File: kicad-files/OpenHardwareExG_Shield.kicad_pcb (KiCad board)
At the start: 4 copper layers, 125.1 x 59.7 mm, 196 parts, among them P1 CONN_1, P10 CONN_18, P11 CONN_1, P12 CONN_1, P13 CONN_1, P14 CONN_1, P15 CONN_1, P16 CONN_1, P17 CONN_1, P18 CONN_1, P19 ARDUINO_SHIELD, P2 CONN_1, P20 CONN_3X2, P21 CONN_3X2, P22 CONN_7, P23 CONN_1, P24 CONN_1, P25 CONN_1, P26 CONN_1, P27 CONN_1, P28 CONN_1, P29 CONN_1, P3 CONN_1, P30 CONN_1, P31 CONN_1, P32 CONN_1, P33 CONN_1, P34 CONN_1, P35 CONN_1, P36 CONN_1, P37 CONN_1, P38 CONN_1, P39 CONN_1, P4 CONN_1, P40 CONN_1, P41 CONN_1, P42 CONN_1, P43 CONN_1, P44 CONN_1, P45 CONN_1, P46 CONN_1, P47 CONN_1, P48 CONN_1, P49 CONN_1, P5 CONN_1, P50 CONN_1, P51 CONN_1, P52 CONN_1, P53 CONN_1, P54 CONN_1, P55 CONN_1, P6 CONN_1, P7 CONN_1, P8 CONN_1, P9 CONN_1, U1 ADS1299, U2 Z0109MNT1G, U3 TL431BIDBZR, U4 873-AAT3220IGY-33T1, U5 ADUM6000, U6 SI8663, U7 74LS02, U8 74LS00, U9 74LS125

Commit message: connect DGND_ISO to DGND (DOH!); convert to KiCad 4
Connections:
- P19 pad 0: (no net) -> Net-(P19-Pad0)
- P19 pad 1: (no net) -> Net-(P19-Pad1)
- P19 pad 10: (no net) -> Net-(P19-Pad10)
- P19 pad 11: (no net) -> Net-(P19-Pad11)
- P19 pad 12: (no net) -> Net-(P19-Pad12)
- P19 pad 13: (no net) -> Net-(P19-Pad13)
- P19 pad 2: (no net) -> Net-(P19-Pad2)
- P19 pad 3: (no net) -> Net-(P19-Pad3)
- P19 pad 4: (no net) -> Net-(P19-Pad4)
- P19 pad 54: (no net) -> Net-(P19-Pad54)
- P19 pad 55: (no net) -> Net-(P19-Pad55)
- P19 pad 56: (no net) -> Net-(P19-Pad56)
- P19 pad 57: (no net) -> Net-(P19-Pad57)
- P19 pad 58: (no net) -> Net-(P19-Pad58)
- P19 pad 59: (no net) -> Net-(P19-Pad59)
- P19 pad 70: (no net) -> Net-(P19-Pad70)
- P19 pad 71: (no net) -> Net-(P19-Pad71)
- P19 pad 8: (no net) -> Net-(P19-Pad8)
- P19 pad 88: (no net) -> Net-(P19-Pad88)
- P19 pad 89: (no net) -> Net-(P19-Pad89)
- P19 pad 9: (no net) -> Net-(P19-Pad9)
- P19 pad 90: (no net) -> Net-(P19-Pad90)
- P19 pad 92: (no net) -> Net-(P19-Pad92)
- P19 pad 97: (no net) -> Net-(P19-Pad97)
- P19 pad 98: (no net) -> Net-(P19-Pad98)
- P22 pad 5: /DGND_ISO -> AGND
- P31 pad 1: /DGND_ISO -> AGND
- U1 pad 17: (no net) -> Net-(U1-Pad17)
- U1 pad 18: (no net) -> Net-(U1-Pad18)
- U1 pad 27: (no net) -> Net-(U1-Pad27)
- U1 pad 29: (no net) -> Net-(U1-Pad29)
- U1 pad 60: (no net) -> Net-(U1-Pad60)
- U1 pad 62: (no net) -> Net-(U1-Pad62)
- U1 pad 64: (no net) -> Net-(U1-Pad64)
- U5 pad 11: (no net) -> Net-(U5-Pad11)
- U5 pad 12: (no net) -> Net-(U5-Pad12)
- U5 pad 4: (no net) -> Net-(U5-Pad4)
- U5 pad 5: (no net) -> Net-(U5-Pad5)
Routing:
- net AGND: track 160.0 -> 162.5 mm
- net /DGND_ISO: track 2.54 -> 0.00 mm

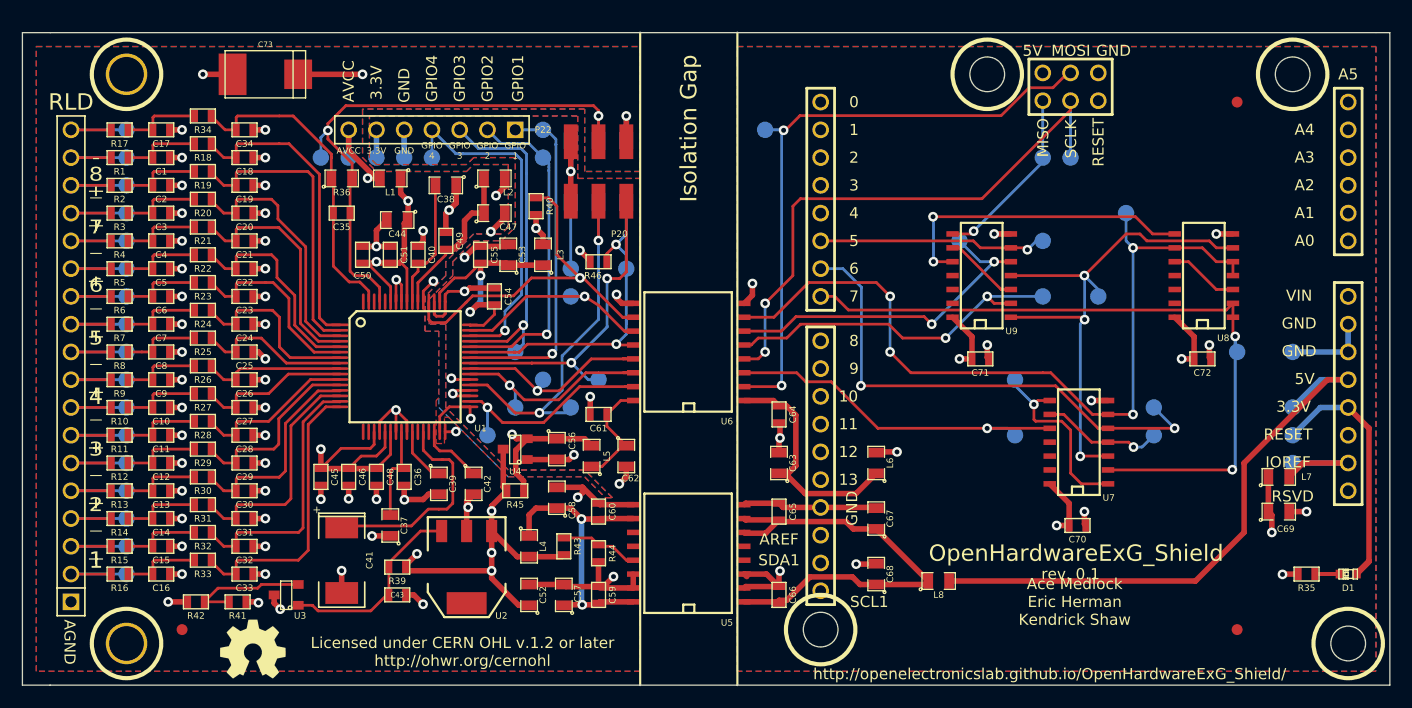
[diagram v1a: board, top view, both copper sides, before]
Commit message: replace fudicial marks with new library modules
removes the paste layer

also added fudicials to the back
and one near the ADS129x
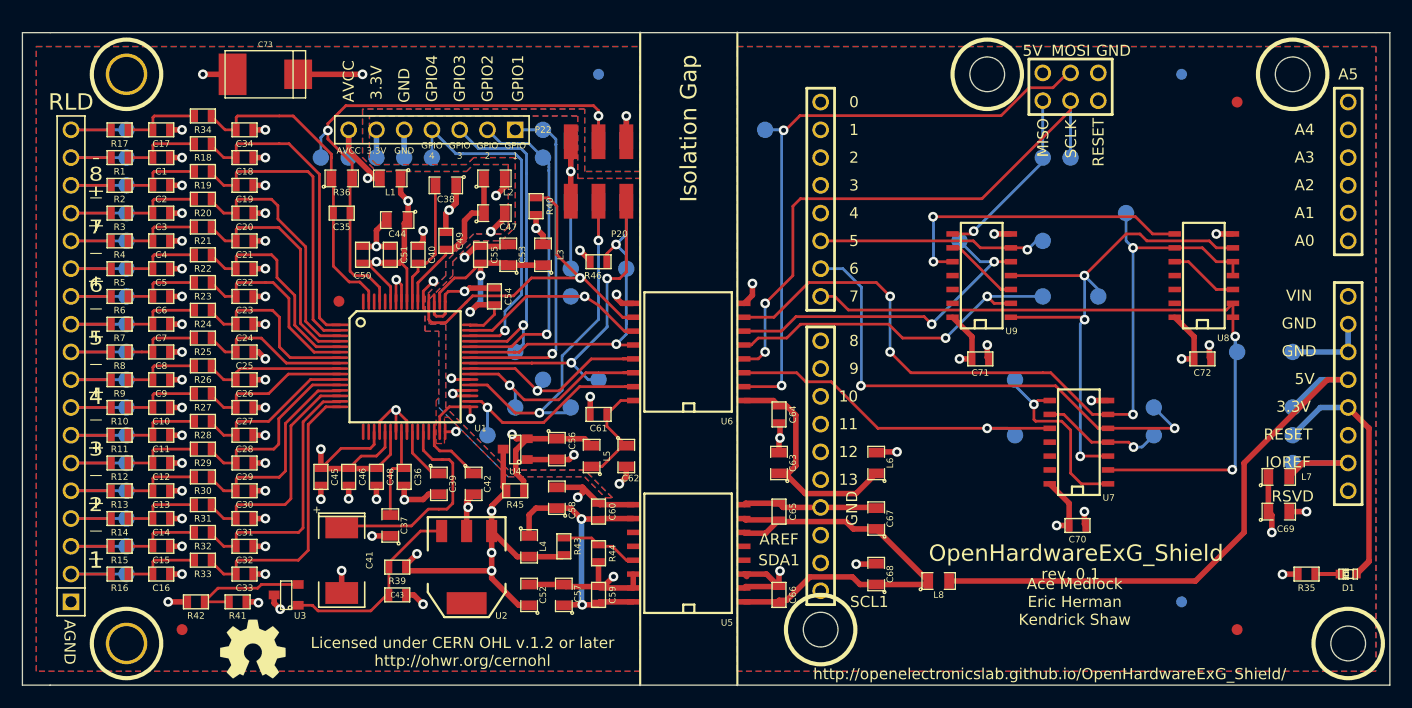
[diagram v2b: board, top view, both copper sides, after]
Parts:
- removed fiducial_mark (x3): VAL**, fiducial_mark
- added REF**: Fiducial_1mm_Dia_2.54mm_Outer_CopperTop, Fiducials:Fiducial_1mm_Dia_2.54mm_Outer_CopperTop, F.Cu at (170.2, 83.8)
- added REF**: Fiducial_1mm_Dia_2.54mm_Outer_CopperTop, Fiducials:Fiducial_1mm_Dia_2.54mm_Outer_CopperTop, B.Cu at (165.1, 81.3)
- added REF**: Fiducial_1mm_Dia_2.54mm_Outer_CopperTop, Fiducials:Fiducial_1mm_Dia_2.54mm_Outer_CopperTop, F.Cu at (170.2, 35.6)
- added REF**: Fiducial_1mm_Dia_2.54mm_Outer_CopperTop, Fiducials:Fiducial_1mm_Dia_2.54mm_Outer_CopperTop, B.Cu at (165.1, 33.0)
- added REF**: Fiducial_1mm_Dia_2.54mm_Outer_CopperTop, Fiducials:Fiducial_1mm_Dia_2.54mm_Outer_CopperTop, F.Cu at (73.7, 83.8)
- added REF**: Fiducial_1mm_Dia_2.54mm_Outer_CopperTop, Fiducials:Fiducial_1mm_Dia_2.54mm_Outer_CopperTop, F.Cu at (88.0, 53.8)
- added REF**: Fiducial_1mm_Dia_2.54mm_Outer_CopperTop, Fiducials:Fiducial_1mm_Dia_2.54mm_Outer_CopperTop, B.Cu at (111.8, 33.0)
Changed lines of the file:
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@@
-(kicad_pcb (version 4) (host pcbnew 4.0.0-2.201511301920+6191~38~ubuntu14.04.1-stable)
+(kicad_pcb (version 4) (host pcbnew 4.0.1-3.201512221402+6198~38~ubuntu14.04.1-stable)
   (general
     (links 375)
     (no_connects 0)
-    (area 59.004999 29.159999 184.200001 88.950001)
+    (area 59.004999 27.7613 184.8367 91.5924)
     (thickness 1.6)
     (drawings 67)
     (tracks 1168)
     (zones 0)
-    (modules 196)
+    (modules 200)
     (nets 141)
   )
@@
     (38 B.Mask user)
     (39 F.Mask user)
-    (40 Dwgs.User user hide)
-    (41 Cmts.User user hide)
-    (42 Eco1.User user hide)
-    (43 Eco2.User user hide)
+    (40 Dwgs.User user)
+    (41 Cmts.User user)
+    (42 Eco1.User user)
+    (43 Eco2.User user)
     (44 Edge.Cuts user)
+    (46 B.CrtYd user)
+    (47 F.CrtYd user)
   )
   (setup
@@
     (mod_text_size 1 1)
     (mod_text_width 0.15)
-    (pad_size 3.7973 3.7973)
-    (pad_drill 3.175)
+    (pad_size 1.00076 1.00076)
+    (pad_drill 0)
     (pad_to_mask_clearance 0)
     (aux_axis_origin 0 0)
     (visible_elements 7FFFFF3F)
     (pcbplotparams
-      (layerselection 0x010fc_80000007)
+      (layerselection 0x0d0fc_80000007)
       (usegerberextensions true)
       (excludeedgelayer true)
@@
     (add_net VCC)
   )
+  (module Fiducials:Fiducial_1mm_Dia_2.54mm_Outer_CopperTop (layer F.Cu)
+    (at 170.18 83.82)
+    (descr "Circular Fiducial, 1mm bare copper top; 2.54mm keepout")
+    (tags marker)
+    (attr virtual)
+    (fp_text reference REF** (at 3.4 0.7) (layer F.SilkS) hide
+      (effects (font (size 1 1) (thickness 0.15)))
+    )
+    (fp_text value Fiducial_1mm_Dia_2.54mm_Outer_CopperTop (at 0 -1.8) (layer F.Fab) hide
+      (effects (font (size 1 1) (thickness 0.15)))
+    )
+    (fp_circle (center 0 0) (end 1.55 0) (layer F.CrtYd) (width 0.05))
+    (pad ~ smd circle (at 0 0) (size 1 1) (layers F.Cu F.Mask)
+      (solder_mask_margin 0.77) (clearance 0.77))
+  )
+  (module Fiducials:Fiducial_1mm_Dia_2.54mm_Outer_CopperTop (layer B.Cu)
+    (at 165.1 81.28)
+    (descr "Circular Fiducial, 1mm bare copper top; 2.54mm keepout")
+    (tags marker)
+    (attr virtual)
+    (fp_text reference REF** (at 3.4 -0.7) (layer B.SilkS) hide
+      (effects (font (size 1 1) (thickness 0.15)) (justify mirror))
+    )
+    (fp_text value Fiducial_1mm_Dia_2.54mm_Outer_CopperTop (at 0 1.8) (layer B.Fab) hide
+      (effects (font (size 1 1) (thickness 0.15)) (justify mirror))
+    )
+    (fp_circle (center 0 0) (end 1.55 0) (layer B.CrtYd) (width 0.05))
+    (pad ~ smd circle (at 0 0) (size 1 1) (layers B.Cu B.Mask)
+      (solder_mask_margin 0.77) (clearance 0.77))
+  )
+  (module Fiducials:Fiducial_1mm_Dia_2.54mm_Outer_CopperTop (layer F.Cu)
+    (at 170.18 35.56)
+    (descr "Circular Fiducial, 1mm bare copper top; 2.54mm keepout")
+    (tags marker)
+    (attr virtual)
+    (fp_text reference REF** (at 3.4 0.7) (layer F.SilkS) hide
+      (effects (font (size 1 1) (thickness 0.15)))
+    )
+    (fp_text value Fiducial_1mm_Dia_2.54mm_Outer_CopperTop (at 0 -1.8) (layer F.Fab) hide
+      (effects (font (size 1 1) (thickness 0.15)))
+    )
+    (fp_circle (center 0 0) (end 1.55 0) (layer F.CrtYd) (width 0.05))
+    (pad ~ smd circle (at 0 0) (size 1 1) (layers F.Cu F.Mask)
+      (solder_mask_margin 0.77) (clearance 0.77))
+  )
+  (module Fiducials:Fiducial_1mm_Dia_2.54mm_Outer_CopperTop (layer B.Cu)
+    (at 165.1 33.02)
+    (descr "Circular Fiducial, 1mm bare copper top; 2.54mm keepout")
+    (tags marker)
+    (attr virtual)
+    (fp_text reference REF** (at 3.4 -0.7) (layer B.SilkS) hide
+      (effects (font (size 1 1) (thickness 0.15)) (justify mirror))
+    )
+    (fp_text value Fiducial_1mm_Dia_2.54mm_Outer_CopperTop (at 0 1.8) (layer B.Fab) hide
+      (effects (font (size 1 1) (thickness 0.15)) (justify mirror))
+    )
+    (fp_circle (center 0 0) (end 1.55 0) (layer B.CrtYd) (width 0.05))
+    (pad ~ smd circle (at 0 0) (size 1 1) (layers B.Cu B.Mask)
+      (solder_mask_margin 0.77) (clearance 0.77))
+  )
+  (module Fiducials:Fiducial_1mm_Dia_2.54mm_Outer_CopperTop (layer F.Cu)
+    (at 73.66 83.82)
+    (descr "Circular Fiducial, 1mm bare copper top; 2.54mm keepout")
+    (tags marker)
+    (attr virtual)
+    (fp_text reference REF** (at 3.4 0.7) (layer F.SilkS) hide
+      (effects (font (size 1 1) (thickness 0.15)))
+    )
+    (fp_text value Fiducial_1mm_Dia_2.54mm_Outer_CopperTop (at 0 -1.8) (layer F.Fab) hide
+      (effects (font (size 1 1) (thickness 0.15)))
+    )
+    (fp_circle (center 0 0) (end 1.55 0) (layer F.CrtYd) (width 0.05))
+    (pad ~ smd circle (at 0 0) (size 1 1) (layers F.Cu F.Mask)
+      (solder_mask_margin 0.77) (clearance 0.77))
+  )
   (module LOGO (layer F.Cu)
     (at 80.137 85.598)
@@
       (net 24 /BIASOUT_FILT))
   )
-  (module fiducial_mark (layer F.Cu)
-    (at 73.66 83.82)
-    (fp_text reference fiducial_mark (at 0 -0.59944) (layer F.SilkS) hide
-      (effects (font (size 0.6 0.6) (thickness 0.127)))
-    )
-    (fp_text value VAL** (at 0 0.8001) (layer F.SilkS) hide
-      (effects (font (size 0.127 0.127) (thickness 0.03048)))
-    )
-    (pad 1 smd circle (at 0 0) (size 1.00076 1.00076) (layers F.Cu F.Paste F.Mask)
-      (solder_mask_margin 0.50038) (clearance 0.50038))
-  )
-  (module fiducial_mark (layer F.Cu)
-    (at 170.18 83.82)
-    (fp_text reference fiducial_mark (at 0 -0.59944) (layer F.SilkS) hide
-      (effects (font (size 0.6 0.6) (thickness 0.127)))
-    )
-    (fp_text value VAL** (at 0 0.8001) (layer F.SilkS) hide
-      (effects (font (size 0.127 0.127) (thickness 0.03048)))
-    )
-    (pad 1 smd circle (at 0 0) (size 1.00076 1.00076) (layers F.Cu F.Paste F.Mask)
-      (solder_mask_margin 0.50038) (clearance 0.50038))
-  )
-  (module fiducial_mark (layer F.Cu)
-    (at 170.18 35.56)
-    (fp_text reference fiducial_mark (at 0 -0.59944) (layer F.SilkS) hide
-      (effects (font (size 0.6 0.6) (thickness 0.127)))
-    )
-    (fp_text value VAL** (at 0 0.8001) (layer F.SilkS) hide
-      (effects (font (size 0.127 0.127) (thickness 0.03048)))
-    )
-    (pad 1 smd circle (at 0 0) (size 1.00076 1.00076) (layers F.Cu F.Paste F.Mask)
-      (solder_mask_margin 0.50038) (clearance 0.50038))
-  )
   (module arduino_shield_with_holes (layer F.Cu)
     (at 154.94 54.61 90)
@@
     )
   )
+  (module Fiducials:Fiducial_1mm_Dia_2.54mm_Outer_CopperTop (layer F.Cu)
+    (at 88.011 53.7845)
+    (descr "Circular Fiducial, 1mm bare copper top; 2.54mm keepout")
+    (tags marker)
+    (attr virtual)
+    (fp_text reference REF** (at 3.4 0.7) (layer F.SilkS) hide
+      (effects (font (size 1 1) (thickness 0.15)))
+    )
+    (fp_text value Fiducial_1mm_Dia_2.54mm_Outer_CopperTop (at 0 -1.8) (layer F.Fab) hide
+      (effects (font (size 1 1) (thickness 0.15)))
+    )
+    (fp_circle (center 0 0) (end 1.55 0) (layer F.CrtYd) (width 0.05))
+    (pad ~ smd circle (at 0 0) (size 1 1) (layers F.Cu F.Mask)
+      (solder_mask_margin 0.77) (clearance 0.77))
+  )
+  (module Fiducials:Fiducial_1mm_Dia_2.54mm_Outer_CopperTop (layer B.Cu)
+    (at 111.76 33.02)
+    (descr "Circular Fiducial, 1mm bare copper top; 2.54mm keepout")
+    (tags marker)
+    (attr virtual)
+    (fp_text reference REF** (at 3.4 -0.7) (layer B.SilkS)
+      (effects (font (size 1 1) (thickness 0.15)) (justify mirror))
+    )
+    (fp_text value Fiducial_1mm_Dia_2.54mm_Outer_CopperTop (at 0 1.8) (layer B.Fab)
+      (effects (font (size 1 1) (thickness 0.15)) (justify mirror))
+    )
+    (fp_circle (center 0 0) (end 1.55 0) (layer B.CrtYd) (width 0.05))
+    (pad ~ smd circle (at 0 0) (size 1 1) (layers B.Cu B.Mask)
+      (solder_mask_margin 0.77) (clearance 0.77))
+  )
   (gr_text "GPIO\n1" (at 104.14 40.005) (layer F.SilkS)

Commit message: bump PCB version to 0.2
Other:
- board text added: "rev. 0.2"
- board text removed: "rev. 0.1"
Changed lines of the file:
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@@
-(kicad_pcb (version 4) (host pcbnew 4.0.1-3.201512221402+6198~38~ubuntu14.04.1-stable)
+(kicad_pcb (version 4) (host pcbnew 4.0.2+e4-6225~38~ubuntu14.04.1-stable)
   (general
     (links 375)
     (no_connects 0)
-    (area 59.004999 27.7613 184.8367 91.5924)
+    (area 56.643704 27.7613 187.196296 91.5924)
     (thickness 1.6)
     (drawings 67)
@@
     (effects (font (size 1.016 1.016) (thickness 0.2032)) (justify mirror))
   )
-  (gr_text "rev. 0.1" (at 154.94 78.74) (layer F.SilkS)
+  (gr_text "rev. 0.2" (at 154.94 78.74) (layer F.SilkS)
     (effects (font (size 1.016 1.016) (thickness 0.2032)))
   )
-  (gr_text "rev. 0.1" (at 154.94 78.74) (layer B.SilkS)
+  (gr_text "rev. 0.2" (at 154.94 78.74) (layer B.SilkS)
     (effects (font (size 1.016 1.016) (thickness 0.2032)) (justify mirror))
   )
